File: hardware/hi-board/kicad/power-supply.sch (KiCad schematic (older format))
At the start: 9 parts, among them U3 TLV61046ADB, U4 ME6216A30M3G

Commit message: Complete display schematic and change footprints
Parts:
- C4, C5, C6, C7: footprint Capacitor_SMD:C_0402_1005Metric -> Capacitor_SMD:C_0603_1608Metric
- R7, R8: footprint Resistor_SMD:R_0402_1005Metric -> Resistor_SMD:R_0603_1608Metric
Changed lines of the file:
@@
 F 0 "C4" H 3342 3396 50  0000 L CNN
 F 1 "1µF" H 3342 3305 50  0000 L CNN
-F 2 "Capacitor_SMD:C_0402_1005Metric" H 3250 3350 50  0001 C CNN
+F 2 "Capacitor_SMD:C_0603_1608Metric" H 3250 3350 50  0001 C CNN
 F 3 "~" H 3250 3350 50  0001 C CNN
 	1    3250 3350
@@
 F 0 "R7" H 4809 3496 50  0000 L CNN
 F 1 "1M" H 4809 3405 50  0000 L CNN
-F 2 "Resistor_SMD:R_0402_1005Metric" H 4750 3450 50  0001 C CNN
+F 2 "Resistor_SMD:R_0603_1608Metric" H 4750 3450 50  0001 C CNN
 F 3 "~" H 4750 3450 50  0001 C CNN
 	1    4750 3450
@@
 F 0 "R8" H 4809 3796 50  0000 L CNN
 F 1 "71.5k" H 4809 3705 50  0000 L CNN
-F 2 "Resistor_SMD:R_0402_1005Metric" H 4750 3750 50  0001 C CNN
+F 2 "Resistor_SMD:R_0603_1608Metric" H 4750 3750 50  0001 C CNN
 F 3 "~" H 4750 3750 50  0001 C CNN
 	1    4750 3750
@@
 F 0 "C5" H 5292 3496 50  0000 L CNN
 F 1 "4.7µF" H 5292 3405 50  0000 L CNN
-F 2 "Capacitor_SMD:C_0402_1005Metric" H 5200 3450 50  0001 C CNN
+F 2 "Capacitor_SMD:C_0603_1608Metric" H 5200 3450 50  0001 C CNN
 F 3 "~" H 5200 3450 50  0001 C CNN
 	1    5200 3450
@@
 F 0 "C6" H 6992 3646 50  0000 L CNN
 F 1 "10µF" H 6992 3555 50  0000 L CNN
-F 2 "Capacitor_SMD:C_0402_1005Metric" H 6900 3600 50  0001 C CNN
+F 2 "Capacitor_SMD:C_0603_1608Metric" H 6900 3600 50  0001 C CNN
 F 3 "~" H 6900 3600 50  0001 C CNN
 	1    6900 3600
@@
 F 0 "C7" H 8142 3646 50  0000 L CNN
 F 1 "10µF" H 8142 3555 50  0000 L CNN
-F 2 "Capacitor_SMD:C_0402_1005Metric" H 8050 3600 50  0001 C CNN
+F 2 "Capacitor_SMD:C_0603_1608Metric" H 8050 3600 50  0001 C CNN
 F 3 "~" H 8050 3600 50  0001 C CNN
 	1    8050 3600

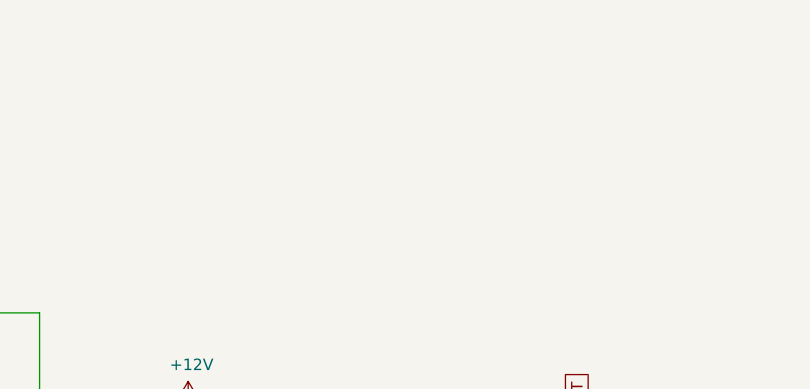
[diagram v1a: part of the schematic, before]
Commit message: Place more caps
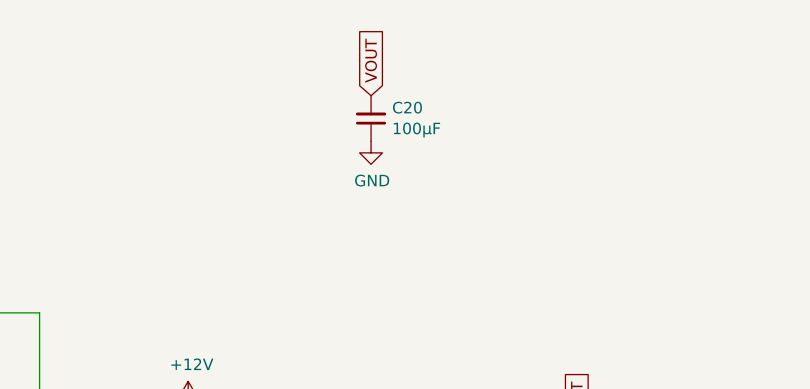
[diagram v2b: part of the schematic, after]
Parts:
- added C20: 100µF, Capacitor_SMD:C_1210_3225Metric, symbol Device:C_Small
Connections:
- net GND: now also C20.1
- net VOUT: now also C20.2
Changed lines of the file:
@@
 Text GLabel 6900 3400 1    50   Input ~ 0
 VOUT
+$Comp
+L Device:C_Small C20
+U 1 1 61645148
+P 6000 2000
+F 0 "C20" H 5908 1954 50  0000 R CNN
+F 1 "100µF" H 5908 2045 50  0000 R CNN
+F 2 "Capacitor_SMD:C_1210_3225Metric" H 6000 2000 50  0001 C CNN
+F 3 "~" H 6000 2000 50  0001 C CNN
+	1    6000 2000
+	-1   0    0    1
+$EndComp
+$Comp
+L power:GND #PWR0205
+U 1 1 6164648E
+P 6000 2100
+F 0 "#PWR0205" H 6000 1850 50  0001 C CNN
+F 1 "GND" H 6005 1927 50  0000 C CNN
+F 2 "" H 6000 2100 50  0001 C CNN
+F 3 "" H 6000 2100 50  0001 C CNN
+	1    6000 2100
+	1    0    0    -1
+$EndComp
+Text GLabel 6000 1900 1    50   Input ~ 0
+VOUT
 $EndSCHEMATC
